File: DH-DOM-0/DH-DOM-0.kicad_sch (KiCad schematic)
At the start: 7 parts, among them SW1 RST, SW2 BOOT, U1 ESP32-S3-WROOM-1

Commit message: Finished Bare Schematic
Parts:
- added C3, C4: 100n, symbol Device:C
- added C5, C6, C7: 10u, symbol Device:C
- added J1: USB_C_Receptacle_USB2.0_14P, symbol Connector:USB_C_Receptacle_USB2.0_14P
- added MMC5983MA: (no value), Package_LGA:LGA-16_3x3mm_P0.5mm, symbol MMC5983MA:MMC5983MA
- added R3, R4: 2.7K, symbol Device:R
- added SSD1306: (no value), symbol SSD_1306:SSD1306
- added U2: (no value), Package_LGA:Bosch_LGA-14_3x2.5mm_P0.5mm, symbol BMI270:BMI270
- added U3: NCP1117-3.3_SOT223, Package_TO_SOT_SMD:SOT-223-3_TabPin2, symbol Regulator_Linear:NCP1117-3.3_SOT223
- added U4: TVS1400DRV, Package_SON:WSON-6-1EP_2x2mm_P0.65mm_EP1x1.6mm, symbol Power_Protection:TVS1400DRV
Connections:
- net +3V3: now also C3.1, C4.1, C7.1, MMC5983MA.13 (VDDIO), MMC5983MA.2 (VDD), R3.1, R4.1, SSD1306.1 (GND), U2.12 (CSB), U2.5 (VDDI0), U2.8 (VDD), U3.2 (VO)
- net D+: now also J1.A6 (D+), J1.B6 (D+)
- net D-: now also J1.A7 (D-), J1.B7 (D-)
- net GND: now also C6.2, C7.2, J1.A1 (GND), J1.A12 (GND), J1.B1 (GND), J1.B12 (GND), J1.SH (SHIELD), SSD1306.2 (VCC), U3.1 (GND), U4.1 (GND), U4.2 (GND), U4.3 (GND), U4.7 (GND)
- net at C1.1, R1.2, SW1.2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: now also C2.1, R2.2, SW2.2, U1.27 (IO0)
- net SDA: now reaches U1.18 (IO10)
- net SDA: now also MMC5983MA.16 (SDA/SDI), R3.2, SSD1306.4 (SDA), U2.14 (SDx)
- net SCL: now reaches U1.19 (IO11)
- net SCL: now also MMC5983MA.1 (SCx), R4.2, SSD1306.3 (SCL), U2.13 (SCx)
- new net: C5.1, MMC5983MA.10 (CAP)
- new net: C3.2, C4.2, C5.2, MMC5983MA.11 (GND), MMC5983MA.8 (GND), U2.1 (SDO), U2.6 (GNDI0), U2.7 (GND)
- new net +5V: C6.1, J1.A4 (VBUS), J1.A9 (VBUS), J1.B4 (VBUS), J1.B9 (VBUS), U3.3 (VI), U4.4 (IN), U4.5 (IN), U4.6 (IN)
- no-connect marks 0 -> 41
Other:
- moved on the sheet: C1, C2, R1, R2, SW1, SW2

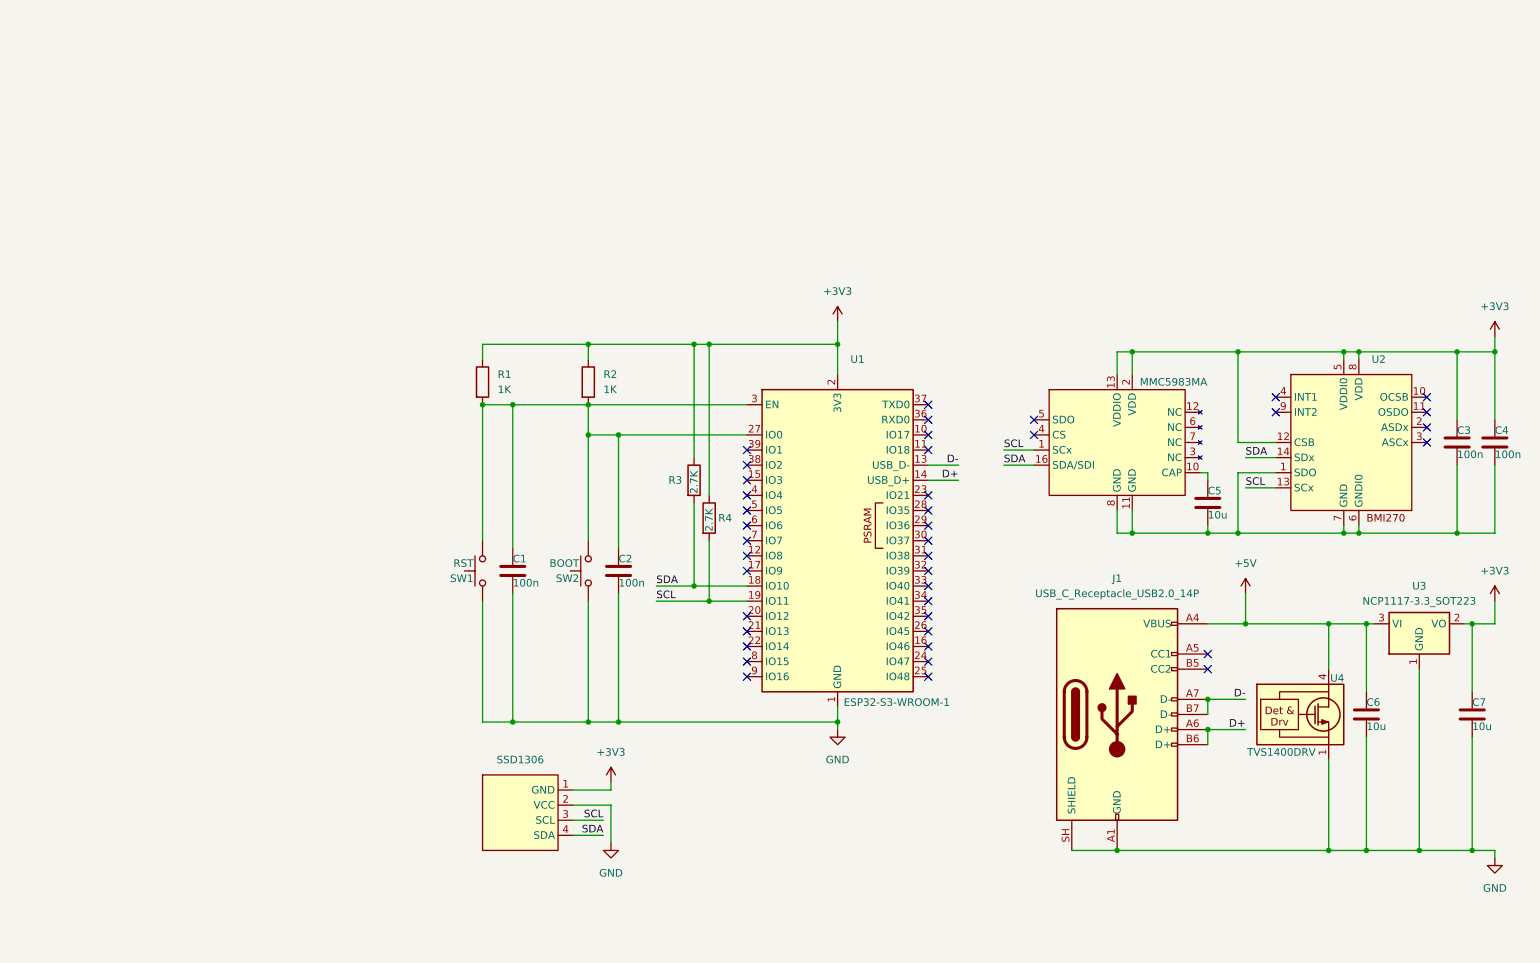
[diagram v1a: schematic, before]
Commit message: fix
fixed wiring error with UI
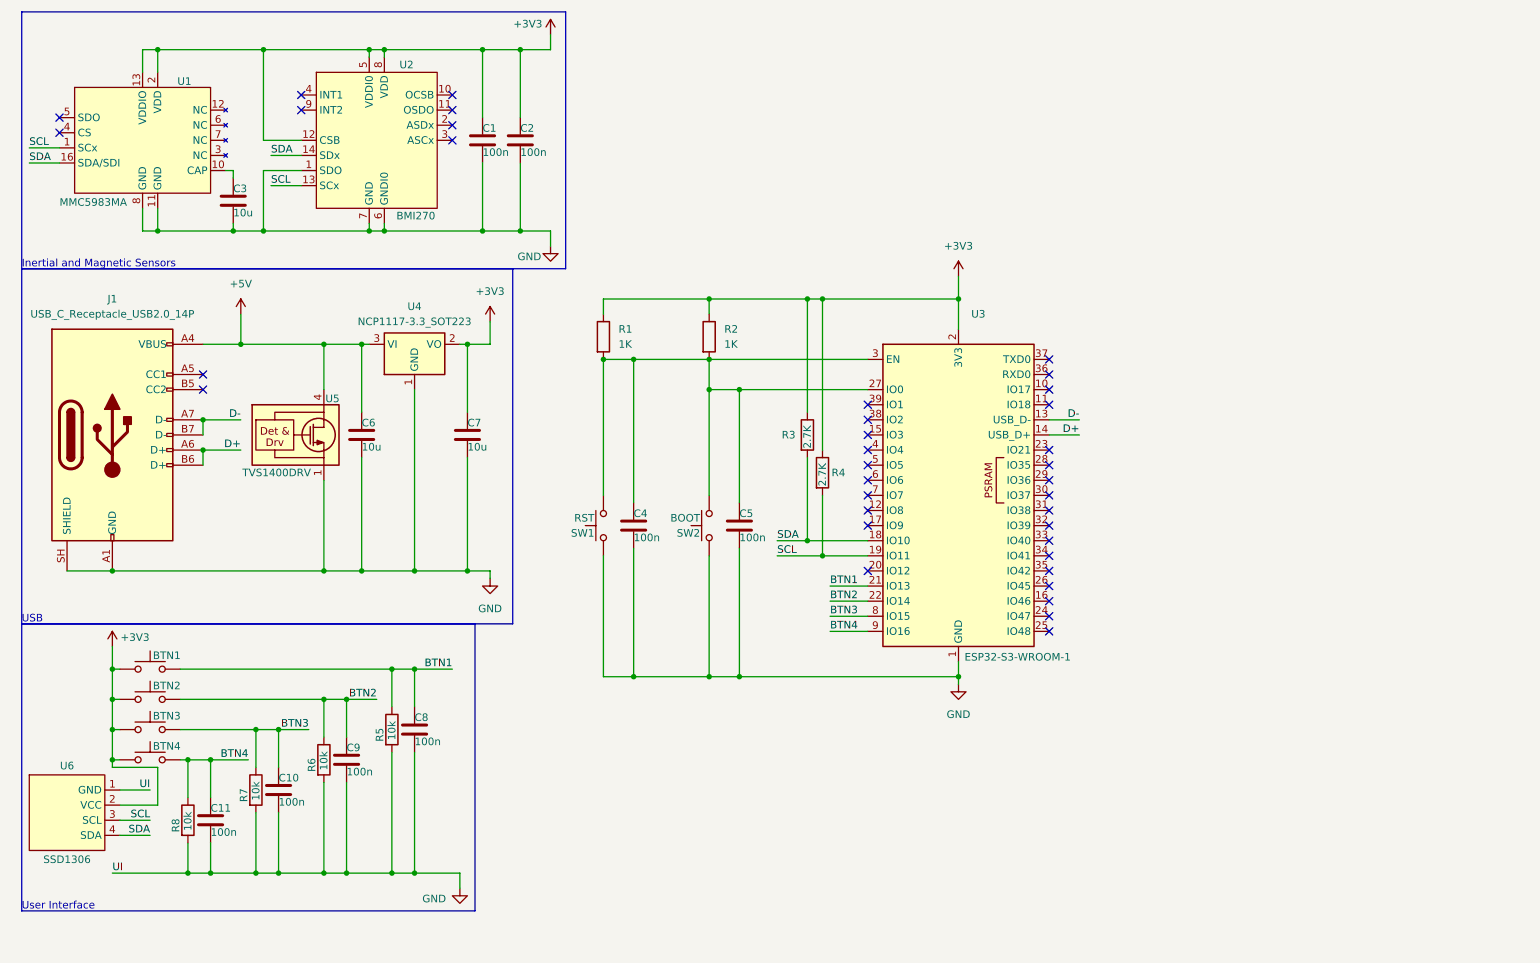
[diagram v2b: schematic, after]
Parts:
- removed MMC5983MA: (no value), Package_LGA:LGA-16_3x3mm_P0.5mm, symbol MMC5983MA:MMC5983MA
- removed SSD1306: (no value), symbol SSD_1306:SSD1306
- added BTN1, BTN2, BTN3, BTN4: SW_Push, Button_Switch_SMD:SW_SPST_PTS645, symbol Switch:SW_Push
- added C10, C11, C8, C9: 100n, Capacitor_SMD:C_0805_2012Metric, symbol Device:C
- added R5, R6, R7, R8: 10k, Resistor_SMD:R_0603_1608Metric, symbol Device:R
- added U1: MMC5983MA, Package_LGA:LGA-16_3x3mm_P0.5mm, symbol MMC5983MA:MMC5983MA
- added U6: SSD1306, Connector_PinSocket_2.54mm:PinSocket_1x04_P2.54mm_Vertical, symbol SSD_1306:SSD1306
- C1: renamed from C3; footprint (none) -> Capacitor_SMD:C_0805_2012Metric
- C2: renamed from C4; footprint (none) -> Capacitor_SMD:C_0805_2012Metric
- C3: renamed from C5; footprint (none) -> Capacitor_SMD:C_0805_2012Metric
- C4: renamed from C1; footprint (none) -> Capacitor_SMD:C_0805_2012Metric
- C5: renamed from C2; footprint (none) -> Capacitor_SMD:C_0805_2012Metric
- C6, C7: footprint (none) -> Capacitor_SMD:C_0805_2012Metric
- J1: footprint (none) -> Connector_USB:USB_C_Receptacle_GCT_USB4105-xx-A_16P_TopMnt_Horizontal
- R1, R2, R3, R4: footprint (none) -> Resistor_SMD:R_0603_1608Metric
- U2: value (none) -> BMI270
- renumbered U1 to U3, U3 to U4, U4 to U5
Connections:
- net +3V3: now also BTN1.1, BTN2.1, BTN3.1, BTN4.1, U1.13 (VDDIO), U1.2 (VDD), U6.2 (VCC)
- net GND: now also C1.2, C2.2, C3.2, U2.1 (SDO), U2.6 (GNDI0), U2.7 (GND), C10.2, C11.2, C8.2, C9.2, R5.2, R6.2, R7.2, R8.2, U1.11 (GND), U1.8 (GND), U6.1 (GND)
- net SCL: now also U1.1 (SCx), U6.3 (SCL)
- net SDA: now also U1.16 (SDA/SDI), U6.4 (SDA)
- net at C3.1: now also U1.10 (CAP)
- net BTN1: now reaches U3.21 (IO13)
- net BTN1: now also BTN1.2, C8.1, R5.1
- net BTN2: now reaches U3.22 (IO14)
- net BTN2: now also BTN2.2, C9.1, R6.1
- net BTN3: now reaches U3.8 (IO15)
- net BTN3: now also BTN3.2, C10.1, R7.1
- net BTN4: now reaches U3.9 (IO16)
- net BTN4: now also BTN4.2, C11.1, R8.1
- no-connect marks 41 -> 37
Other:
- note added: "Inertial and Magnetic Sensors"
- note added: "USB"
- note added: "User Interface"
- moved on the sheet: C1, C2, C3, C4, C5, C6, C7, J1, R1, R2, R3, R4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

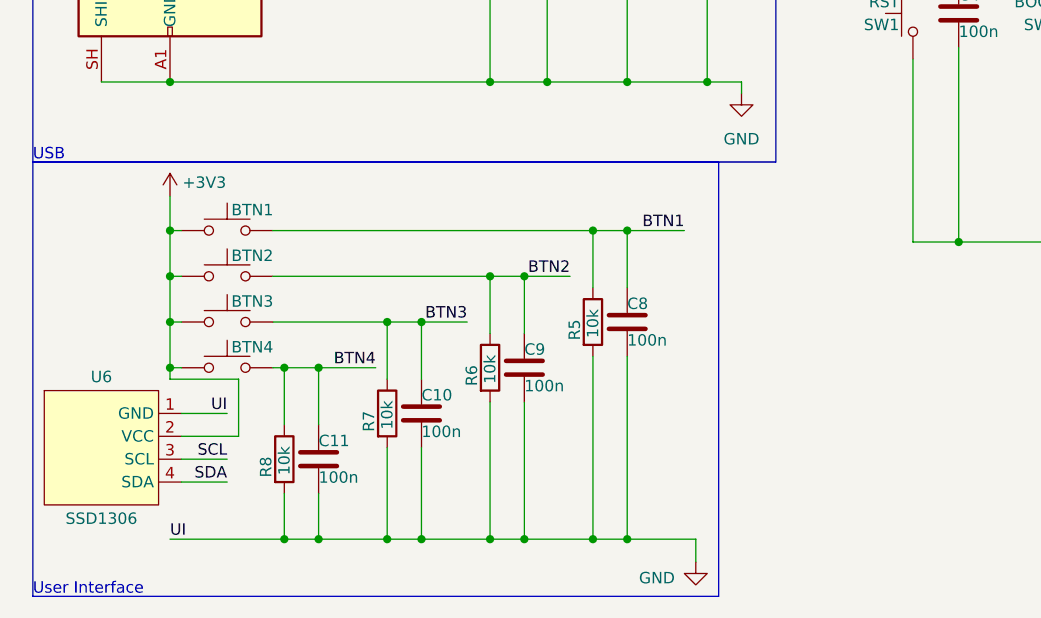
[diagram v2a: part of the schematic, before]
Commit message: edit
+ changed ssd1306 from normal footprint to through hole component for later prototyping and more flexible wiring in final
- ERC errors
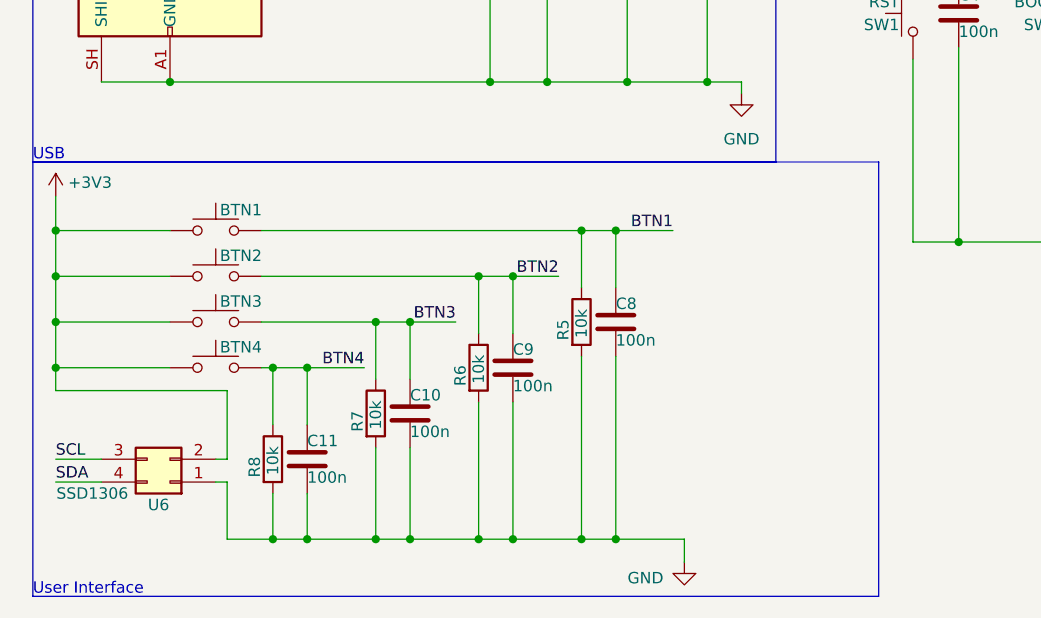
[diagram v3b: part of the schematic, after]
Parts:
- removed U6: SSD1306, Connector_PinSocket_2.54mm:PinSocket_1x04_P2.54mm_Vertical, symbol SSD_1306:SSD1306
- added U6: SSD1306, symbol Connector_Generic:Conn_02x02_Counter_Clockwise
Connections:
- net +3V3: now also U6.2 (Pin_2)
- net GND: now also U6.1 (Pin_1)
- net SCL: now also U6.3 (Pin_3)
- net SDA: now also U6.4 (Pin_4)
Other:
- moved on the sheet: BTN1, BTN2, BTN3, BTN4, C10, C11, C8, C9, R5, R6, R7, R8

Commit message: pcb finish
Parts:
- BTN1, BTN2, BTN3, BTN4: footprint Button_Switch_SMD:SW_SPST_PTS645 -> Connector_PinHeader_1.00mm:PinHeader_2x01_P1.00mm_Vertical
- SW1, SW2: footprint (none) -> Button_Switch_SMD:SW_Push_1P1T_NO_CK_KMR2
- U6: footprint (none) -> Connector_PinSocket_2.54mm:PinSocket_1x04_P2.54mm_Vertical
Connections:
- net BTN1: now also U3.28 (IO35); no longer U3.21 (IO13)
- net BTN2: now also U3.33 (IO40); no longer U3.22 (IO14)
- net BTN3: now also U3.38 (IO2); no longer U3.8 (IO15)
- net BTN4: now also U3.26 (IO45); no longer U3.9 (IO16)
- net GND: now also J1.A5 (CC1), J1.B5 (CC2)
- no-connect marks 37 -> 35
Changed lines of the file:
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@@
 	)
 	(junction
+		(at 45.72 106.68)
+		(diameter 0)
+		(color 0 0 0 0)
+	)
+	(junction
 		(at 115.57 71.12)
 		(diameter 0)
@@
 	)
 	(junction
+		(at 45.72 76.2)
+		(diameter 0)
+		(color 0 0 0 0)
+	)
+	(junction
 		(at 73.66 19.05)
 		(diameter 0)
@@
 	)
 	(no_connect
-		(at 185.42 101.6)
-	)
-	(no_connect
-		(at 185.42 104.14)
-	)
-	(no_connect
-		(at 185.42 99.06)
+		(at 154.94 111.76)
 	)
 	(no_connect
@@
 	)
 	(no_connect
-		(at 43.18 73.66)
-	)
-	(no_connect
-		(at 154.94 81.28)
-	)
-	(no_connect
 		(at 185.42 71.12)
 	)
@@
 	)
 	(no_connect
-		(at 43.18 76.2)
-	)
-	(no_connect
 		(at 154.94 96.52)
 	)
@@
 	)
 	(no_connect
+		(at 154.94 109.22)
+	)
+	(no_connect
 		(at 154.94 78.74)
 	)
@@
 	)
 	(no_connect
-		(at 185.42 93.98)
-	)
-	(no_connect
 		(at 154.94 83.82)
 	)
@@
 	)
 	(no_connect
+		(at 154.94 116.84)
+	)
+	(no_connect
 		(at 185.42 106.68)
 	)
@@
 	)
 	(no_connect
-		(at 185.42 96.52)
+		(at 154.94 114.3)
 	)
 	(no_connect
-		(at 185.42 109.22)
+		(at 185.42 104.14)
 	)
 	(no_connect
-		(at 85.09 31.75)
+		(at 185.42 96.52)
+	)
+	(no_connect
+		(at 185.42 93.98)
 	)
 	(no_connect
-		(at 185.42 88.9)
+		(at 85.09 31.75)
 	)
 	(no_connect
@@
 		(at 185.42 78.74)
 	)
+	(no_connect
+		(at 185.42 99.06)
+	)
 	(wire
 		(pts
@@
 	(wire
 		(pts
+			(xy 43.18 76.2) (xy 45.72 76.2)
+		)
+		(stroke
+			(width 0)
+			(type default)
+		)
+	)
+	(wire
+		(pts
 			(xy 15.24 133.35) (xy 27.94 133.35)
 		)
@@
 	(wire
 		(pts
-			(xy 148.59 111.76) (xy 154.94 111.76)
+			(xy 191.77 101.6) (xy 185.42 101.6)
 		)
 		(stroke
@@
 	(wire
 		(pts
-			(xy 148.59 114.3) (xy 154.94 114.3)
+			(xy 148.59 81.28) (xy 154.94 81.28)
 		)
 		(stroke
@@
 	(wire
 		(pts
-			(xy 148.59 109.22) (xy 154.94 109.22)
+			(xy 191.77 88.9) (xy 185.42 88.9)
 		)
 		(stroke
@@
 	(wire
 		(pts
+			(xy 45.72 76.2) (xy 45.72 106.68)
+		)
+		(stroke
+			(width 0)
+			(type default)
+		)
+	)
+	(wire
+		(pts
 			(xy 128.27 60.96) (xy 144.78 60.96)
 		)
@@
 	(wire
 		(pts
+			(xy 43.18 73.66) (xy 45.72 73.66)
+		)
+		(stroke
+			(width 0)
+			(type default)
+		)
+	)
+	(wire
+		(pts
 			(xy 53.34 34.29) (xy 59.69 34.29)
 		)
@@
 	(wire
 		(pts
+			(xy 45.72 106.68) (xy 63.5 106.68)
+		)
+		(stroke
+			(width 0)
+			(type default)
+		)
+	)
+	(wire
+		(pts
 			(xy 139.7 101.6) (xy 144.78 101.6)
 		)
@@
 	(wire
 		(pts
-			(xy 148.59 116.84) (xy 154.94 116.84)
+			(xy 191.77 109.22) (xy 185.42 109.22)
 		)
 		(stroke
@@
 	(wire
 		(pts
+			(xy 45.72 73.66) (xy 45.72 76.2)
+		)
+		(stroke
+			(width 0)
+			(type default)
+		)
+	)
+	(wire
+		(pts
 			(xy 69.85 87.63) (xy 69.85 106.68)
 		)
@@
 	(wire
 		(pts
-			(xy 27.94 106.68) (xy 63.5 106.68)
+			(xy 27.94 106.68) (xy 45.72 106.68)
 		)
 		(stroke
@@
 	)
 	(label "BTN4"
-		(at 148.59 116.84 0)
+		(at 191.77 109.22 180)
 		(effects
 			(font
 				(size 1.27 1.27)
 			)
-			(justify left bottom)
+			(justify right bottom)
 		)
 	)
@@
 	)
 	(label "BTN1"
-		(at 148.59 109.22 0)
+		(at 191.77 88.9 180)
 		(effects
 			(font
 				(size 1.27 1.27)
 			)
-			(justify left bottom)
+			(justify right bottom)
 		)
 	)
@@
 	)
 	(label "BTN2"
-		(at 148.59 111.76 0)
+		(at 191.77 101.6 180)
 		(effects
 			(font
 				(size 1.27 1.27)
 			)
-			(justify left bottom)
+			(justify right bottom)
 		)
 	)
@@
 	)
 	(label "BTN3"
-		(at 148.59 114.3 0)
+		(at 148.59 81.28 0)
 		(effects
 			(font
@@
 			)
 		)
-		(property "Footprint" ""
+		(property "Footprint" "Button_Switch_SMD:SW_Push_1P1T_NO_CK_KMR2"
 			(at 105.41 99.06 0)
 			(hide yes)
@@
 			)
 		)
-		(property "Footprint" ""
+		(property "Footprint" "Connector_PinSocket_2.54mm:PinSocket_1x04_P2.54mm_Vertical"
 			(at 27.94 151.13 0)
 			(hide yes)
@@
 			)
 		)
-		(property "Footprint" "Button_Switch_SMD:SW_SPST_PTS645"
+		(property "Footprint" "Connector_PinHeader_1.00mm:PinHeader_2x01_P1.00mm_Vertical"
 			(at 33.02 123.19 0)
 			(hide yes)
@@
 			)
 		)
-		(property "Footprint" "Button_Switch_SMD:SW_SPST_PTS645"
+		(property "Footprint" "Connector_PinHeader_1.00mm:PinHeader_2x01_P1.00mm_Vertical"
 			(at 33.02 133.35 0)
 			(hide yes)
@@
 			)
 		)
-		(property "Footprint" "Button_Switch_SMD:SW_SPST_PTS645"
+		(property "Footprint" "Connector_PinHeader_1.00mm:PinHeader_2x01_P1.00mm_Vertical"
 			(at 33.02 118.11 0)
 			(hide yes)
@@
 			)
 		)
-		(property "Footprint" "Button_Switch_SMD:SW_SPST_PTS645"
+		(property "Footprint" "Connector_PinHeader_1.00mm:PinHeader_2x01_P1.00mm_Vertical"
 			(at 33.02 128.27 0)
 			(hide yes)
@@
 			)
 		)
-		(property "Footprint" ""
+		(property "Footprint" "Button_Switch_SMD:SW_Push_1P1T_NO_CK_KMR2"
 			(at 123.19 99.06 0)
 			(hide yes)

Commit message: added bom
new bom
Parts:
- BTN1, BTN2, BTN3, BTN4: footprint Connector_PinHeader_1.00mm:PinHeader_2x01_P1.00mm_Vertical -> Connector_PinHeader_2.54mm:PinHeader_2x01_P2.54mm_Vertical
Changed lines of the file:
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@@
 			)
 		)
-		(property "Footprint" "Connector_PinHeader_1.00mm:PinHeader_2x01_P1.00mm_Vertical"
+		(property "Footprint" "Connector_PinHeader_2.54mm:PinHeader_2x01_P2.54mm_Vertical"
 			(at 33.02 123.19 0)
 			(hide yes)
@@
 			)
 		)
-		(property "Footprint" "Connector_PinHeader_1.00mm:PinHeader_2x01_P1.00mm_Vertical"
+		(property "Footprint" "Connector_PinHeader_2.54mm:PinHeader_2x01_P2.54mm_Vertical"
 			(at 33.02 133.35 0)
 			(hide yes)
@@
 			)
 		)
-		(property "Footprint" "Connector_PinHeader_1.00mm:PinHeader_2x01_P1.00mm_Vertical"
+		(property "Footprint" "Connector_PinHeader_2.54mm:PinHeader_2x01_P2.54mm_Vertical"
 			(at 33.02 118.11 0)
 			(hide yes)
@@
 			)
 		)
-		(property "Footprint" "Connector_PinHeader_1.00mm:PinHeader_2x01_P1.00mm_Vertical"
+		(property "Footprint" "Connector_PinHeader_2.54mm:PinHeader_2x01_P2.54mm_Vertical"
 			(at 33.02 128.27 0)
 			(hide yes)

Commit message: edit
new imu, new footprint, edited schematic, new pcb, old one saved as I2C
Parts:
- removed R3, R4: 2.7K, Resistor_SMD:R_0603_1608Metric, symbol Device:R
- removed U2: BMI270, Package_LGA:Bosch_LGA-14_3x2.5mm_P0.5mm, symbol BMI270:BMI270
- removed U6: SSD1306, Connector_PinSocket_2.54mm:PinSocket_1x04_P2.54mm_Vertical, symbol Connector_Generic:Conn_02x02_Counter_Clockwise
- added U2: LSM6DSOXTR, Package_LGA:LGA-14_3x2.5mm_P0.5mm_LayoutBorder3x4y, symbol 2026-04-26_18-16-28:LSM6DSOXTR
- added U7: ST7789, Connector_PinSocket_2.54mm:PinSocket_1x08_P2.54mm_Vertical, symbol Connector_Generic:Conn_01x08
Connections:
- net +3V3: now also U2.5 (VDDIO), U2.8 (VDD), U7.2 (Pin_2)
- net BTN1: now also U3.32 (IO39); no longer U3.28 (IO35)
- net BTN3: now also U3.34 (IO41); no longer U3.38 (IO2)
- net BTN4: now also U3.35 (IO42); no longer U3.26 (IO45)
- net GND: now also U2.6 (GND), U2.7 (GND), U7.1 (Pin_1)
- net at C4.1, R1.2, SW1.2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: no longer C5.1, R2.2, SW2.2, U3.27 (IO0)
- net MOSI_IMU: now reaches U3.15 (IO3)
- net MOSI_IMU: now also U2.1 (MOSI)
- net MISO_IMU: now reaches U3.16 (IO46)
- net MISO_IMU: now also U2.14 (MISO)
- net SCLK_IMU: now reaches U3.17 (IO9)
- net SCLK_IMU: now also U2.13 (SCLK)
- net SS_MAG: now reaches U3.20 (IO12)
- net SS_MAG: now also U1.4 (SS)
- net SCLK_MAG: now reaches U3.21 (IO13)
- net SCLK_MAG: now also U1.1 (SCx)
- net MOSI_MAG: now reaches U3.22 (IO14)
- net MOSI_MAG: now also U1.16 (MOSI)
- net MISO_MAG: now reaches U1.5 (MISO)
- net MISO_MAG: now also U3.19 (IO11)
- removed net SCL: U1.1 (SCx), U3.19 (IO11)
- net SDA renamed SS_IMU
- net SS_IMU: now also U2.12 (SS); no longer U1.16 (SDA/SDI)
- new net: C5.1, R2.2, SW2.2, U3.27 (IO0)
- new net BACKLIGHT: U7.8 (Pin_8)
- new net D/C: U7.6 (Pin_6)
- new net MOSI: U7.4 (Pin_4)
- new net RESET: U7.5 (Pin_5)
- new net SCLK: U7.3 (Pin_3)
- new net SS: U7.7 (Pin_7)
- no-connect marks 35 -> 27
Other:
- moved on the sheet: C1, C2, C3, R1, R2, U1
